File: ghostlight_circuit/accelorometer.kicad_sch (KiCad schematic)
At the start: 3 parts

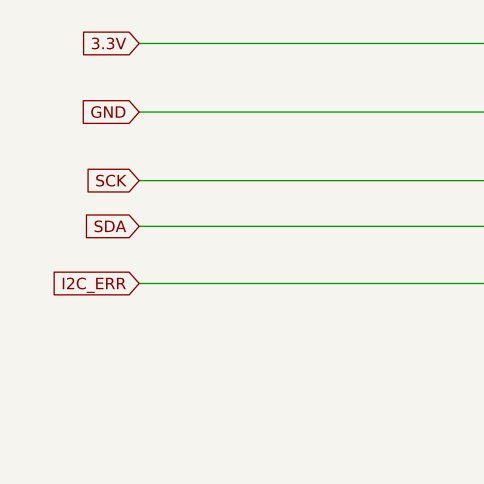
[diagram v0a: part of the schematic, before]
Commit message: update pcb
rerout and connect accelerometer

better re-route
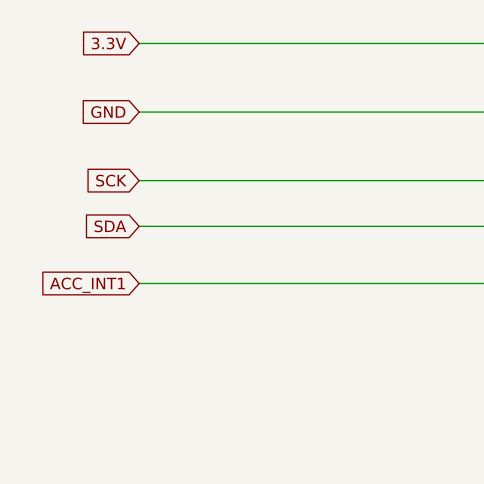
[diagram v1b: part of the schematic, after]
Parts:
- C6: footprint CAPC1005X70N -> Capacitor_SMD:C_0402_1005Metric_Pad0.74x0.62mm_HandSolder
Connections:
- net I2C_ERR renamed ACC_INT1
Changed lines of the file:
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@@
+	)
+	(no_connect
+		(at 189.23 73.66)
 	)
 	(no_connect
@@
 	(no_connect
 		(at 209.55 99.06)
-	)
-	(no_connect
-		(at 189.23 73.66)
 	)
 	(no_connect
@@
 		)
 	)
-	(global_label "I2C_ERR"
-		(shape input)
-		(at 59.69 115.57 180)
-		(fields_autoplaced yes)
-		(effects
-			(font
-				(size 1.27 1.27)
-			)
-			(justify right)
-		)
-		(property "Intersheetrefs" "${INTERSHEET_REFS}"
-			(at 48.9639 115.57 0)
-			(hide yes)
-			(show_name no)
-			(do_not_autoplace no)
-			(effects
-				(font
-					(size 1.27 1.27)
-				)
-				(justify right)
-			)
-		)
-	)
 	(global_label "SDA"
 		(shape input)
@@
 		(property "Intersheetrefs" "${INTERSHEET_REFS}"
 			(at 53.1367 109.22 0)
+			(hide yes)
+			(show_name no)
+			(do_not_autoplace no)
+			(effects
+				(font
+					(size 1.27 1.27)
+				)
+				(justify right)
+			)
+		)
+	)
+	(global_label "ACC_INT1"
+		(shape input)
+		(at 59.69 115.57 180)
+		(fields_autoplaced yes)
+		(effects
+			(font
+				(size 1.27 1.27)
+			)
+			(justify right)
+		)
+		(property "Intersheetrefs" "${INTERSHEET_REFS}"
+			(at 47.9962 115.57 0)
 			(hide yes)
 			(show_name no)
@@
 			)
 		)
-		(property "Footprint" "CAPC1005X70N"
+		(property "Footprint" "Capacitor_SMD:C_0402_1005Metric_Pad0.74x0.62mm_HandSolder"
 			(at 162.56 174.93 0)
 			(hide yes)
